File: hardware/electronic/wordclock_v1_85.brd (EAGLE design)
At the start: 92.6 x 61.5 mm, 29 parts, among them IC3* REG1117, Q1* BS170

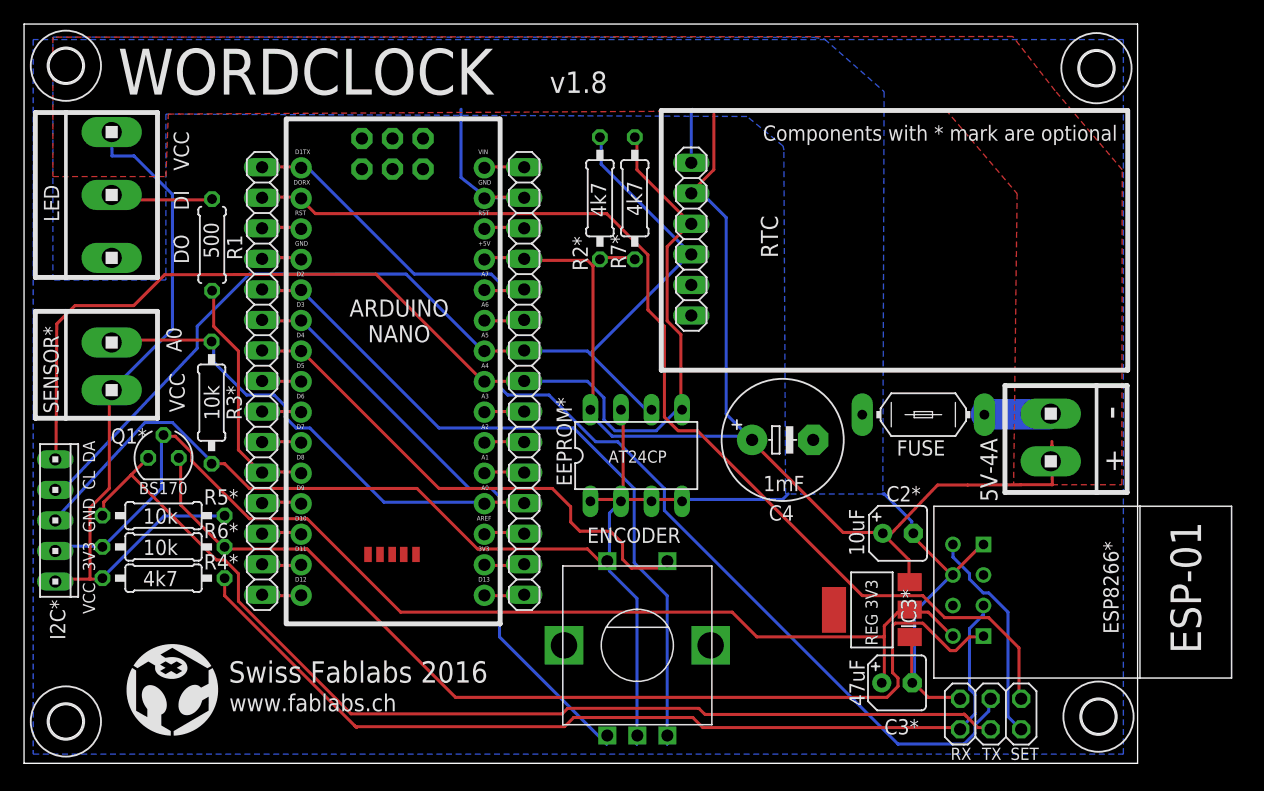
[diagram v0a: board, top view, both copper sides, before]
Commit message: Plans de masse
- Correction des plans de masse
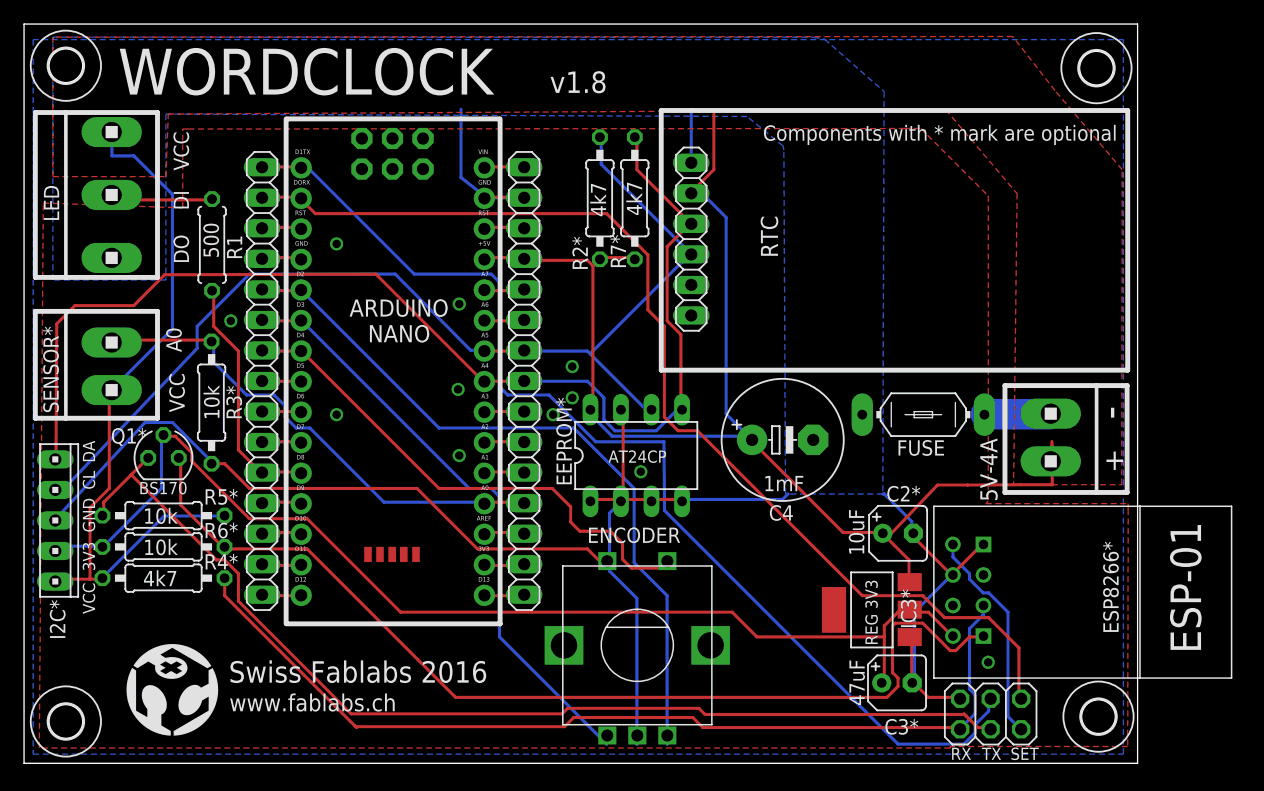
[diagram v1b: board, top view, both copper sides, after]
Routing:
- net N$11: track 89.2 -> 91.4 mm
- net GND: vias 0 -> 11
- added copper zone on layer 1, net GND
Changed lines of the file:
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@@
 <setting verticaltext="up"/>
 </settings>
-<grid distance="0.054" unitdist="mm" unit="mm" style="lines" multiple="1" display="no" altdistance="0.025" altunitdist="inch" altunit="inch"/>
+<grid distance="0.05" unitdist="mm" unit="mm" style="lines" multiple="1" display="yes" altdistance="0.025" altunitdist="inch" altunit="inch"/>
 <layers>
 <layer number="1" name="Top" color="4" fill="1" visible="yes" active="yes"/>
@@
 <vertex x="91.44" y="60.198"/>
 </polygon>
+<polygon width="0.254" layer="1">
+<vertex x="13.67" y="52.76"/>
+<vertex x="73.2" y="52.8"/>
+<vertex x="74.6" y="52.8"/>
+<vertex x="80.2" y="47.2"/>
+<vertex x="80.2" y="21.8"/>
+<vertex x="80" y="21.6"/>
+<vertex x="91.84" y="21.6"/>
+<vertex x="91.84" y="21.16"/>
+<vertex x="91.8" y="1.4"/>
+<vertex x="77.04" y="1.4"/>
+<vertex x="77.04" y="1.27"/>
+<vertex x="1.27" y="1.27"/>
+<vertex x="1.6" y="46.6"/>
+<vertex x="13.2" y="46.2"/>
+<vertex x="13.2" y="52.76"/>
+</polygon>
+<via x="36.1" y="31.1" extent="1-16" drill="0.7"/>
+<via x="36.2" y="38.2" extent="1-16" drill="0.7"/>
+<via x="36.2" y="25.6" extent="1-16" drill="0.7"/>
+<via x="26" y="29" extent="1-16" drill="0.7"/>
+<via x="26" y="43.2" extent="1-16" drill="0.7"/>
+<via x="17.2" y="36.8" extent="1-16" drill="0.7"/>
+<via x="80.2" y="8.4" extent="1-16" drill="0.7"/>
+<via x="45.6" y="33" extent="1-16" drill="0.7"/>
+<via x="45.6" y="30.4" extent="1-16" drill="0.7"/>
+<via x="44" y="29" extent="1-16" drill="0.7"/>
+<via x="51.3" y="24.25" extent="1-16" drill="0.7"/>
 </signal>
 <signal name="VCC">
@@
 <wire x1="53.2638" y1="21.0312" x2="72.6948" y2="1.6002" width="0.254" layer="16"/>
 <wire x1="53.2638" y1="22.86" x2="53.2638" y2="21.0312" width="0.254" layer="16"/>
-<wire x1="49.3776" y1="26.7462" x2="53.2638" y2="22.86" width="0.254" layer="16"/>
-<wire x1="47.5488" y1="26.7462" x2="49.3776" y2="26.7462" width="0.254" layer="16"/>
+<wire x1="53.2276" y1="26.7462" x2="53.2638" y2="22.86" width="0.254" layer="16"/>
+<wire x1="47.5488" y1="26.7462" x2="53.2276" y2="26.7462" width="0.254" layer="16"/>
 <wire x1="43.6626" y1="30.6324" x2="47.5488" y2="26.7462" width="0.254" layer="16"/>
 <wire x1="40.2336" y1="30.6324" x2="43.6626" y2="30.6324" width="0.254" layer="16"/>
@@
 <wire x1="14.4018" y1="36.3474" x2="14.4018" y2="34.5186" width="0.254" layer="16"/>
 <wire x1="18.7452" y1="40.6908" x2="14.4018" y2="36.3474" width="0.254" layer="16"/>
-<wire x1="31.7754" y1="40.6908" x2="18.7452" y2="40.6908" width="0.254" layer="16"/>
-<wire x1="38.1762" y1="34.29" x2="31.7754" y2="40.6908" width="0.254" layer="16"/>
+<wire x1="30.8754" y1="40.6908" x2="18.7452" y2="40.6908" width="0.254" layer="16"/>
+<wire x1="38.1762" y1="34.29" x2="38.1162" y2="34.35" width="0.254" layer="16"/>
+<wire x1="38.1162" y1="34.35" x2="37.15" y2="34.35" width="0.254" layer="16"/>
+<wire x1="37.15" y1="34.35" x2="30.8754" y2="40.6908" width="0.254" layer="16"/>
 <wire x1="2.6574" y1="22.86" x2="2.6" y2="22.74" width="0.254" layer="16"/>
 <wire x1="38.1762" y1="34.29" x2="38.29" y2="34.29" width="0.254" layer="16"/>
